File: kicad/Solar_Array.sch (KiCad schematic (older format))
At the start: 26 parts, among them IC1 SPV1040, P1 PV_CELL, P2 CONN_01X07, Q1 Q_NPN_BCE, U1 LTC2990

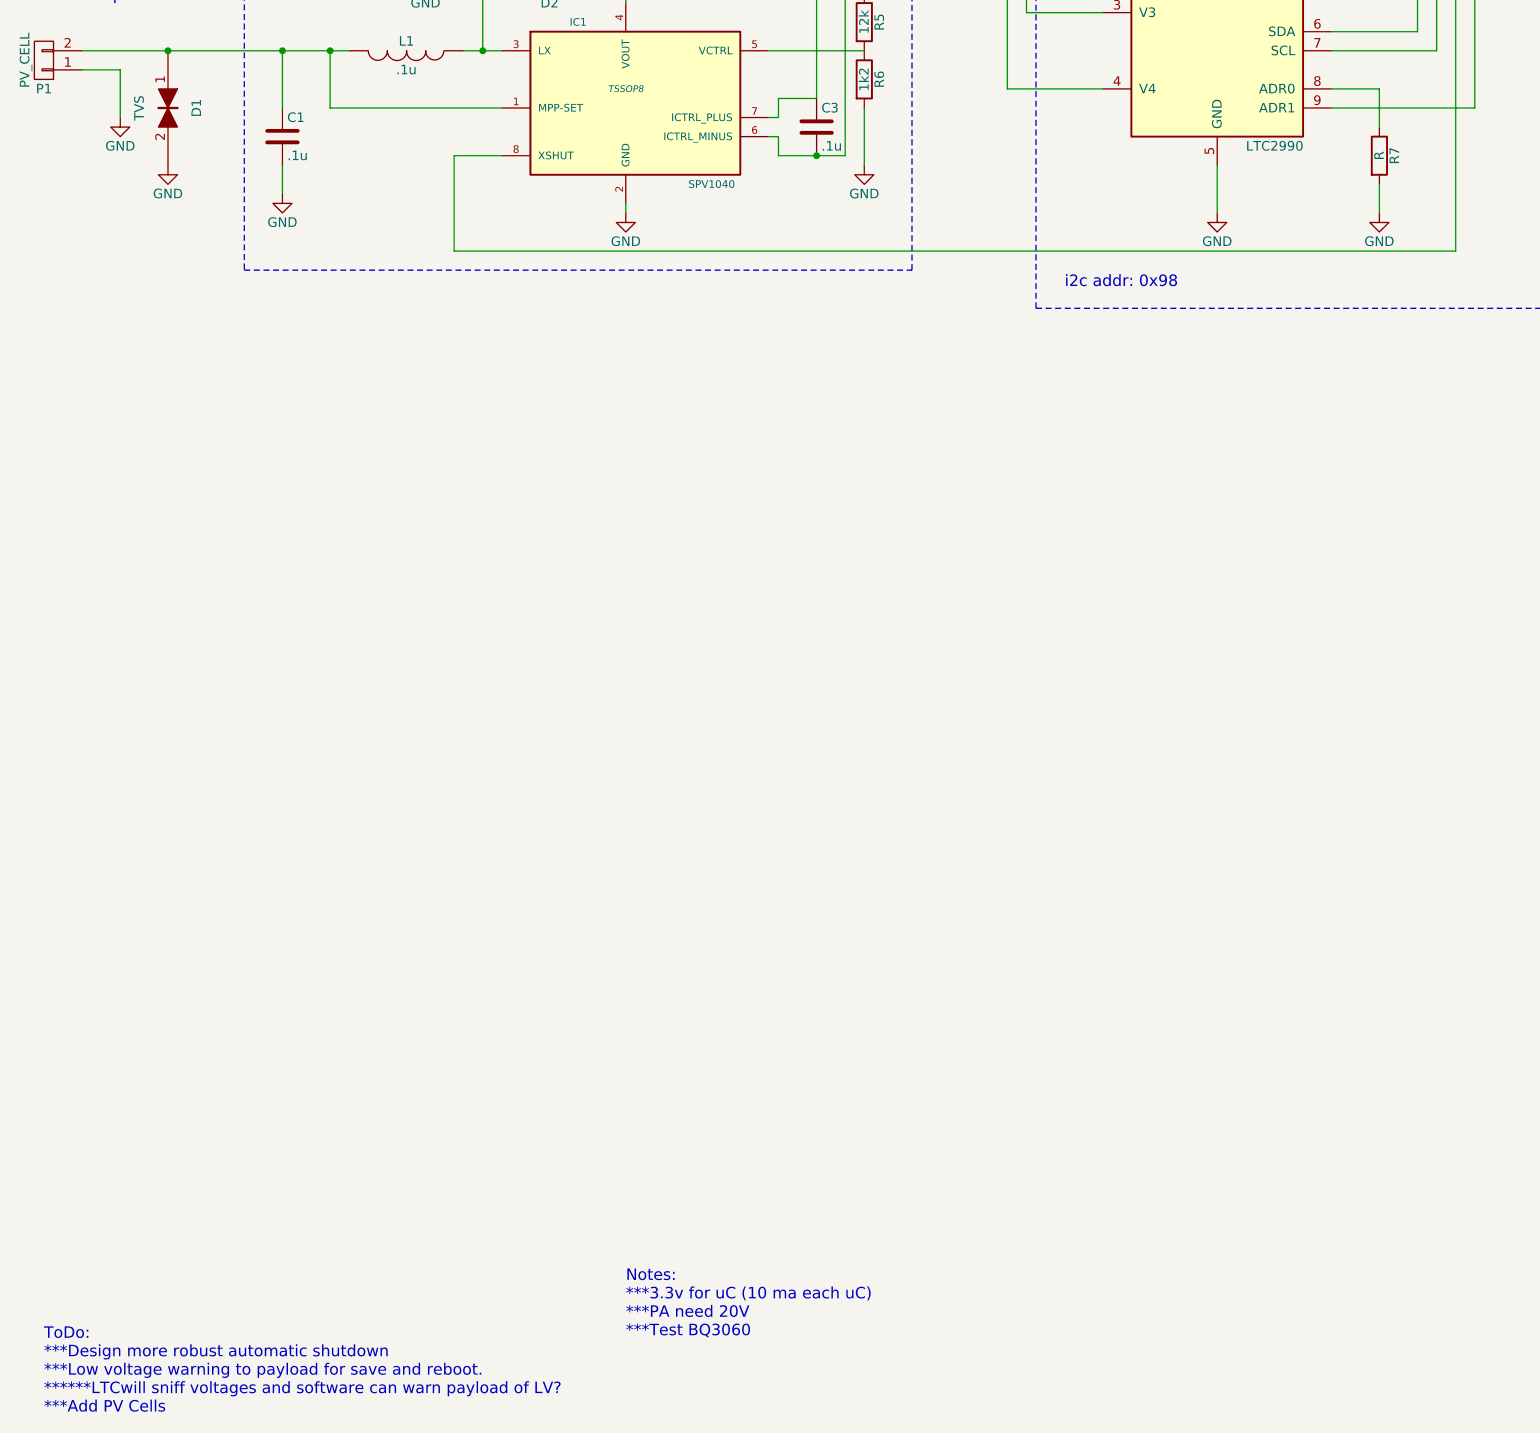
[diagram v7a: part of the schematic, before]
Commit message: Update component values, generated netlist, changed notes.
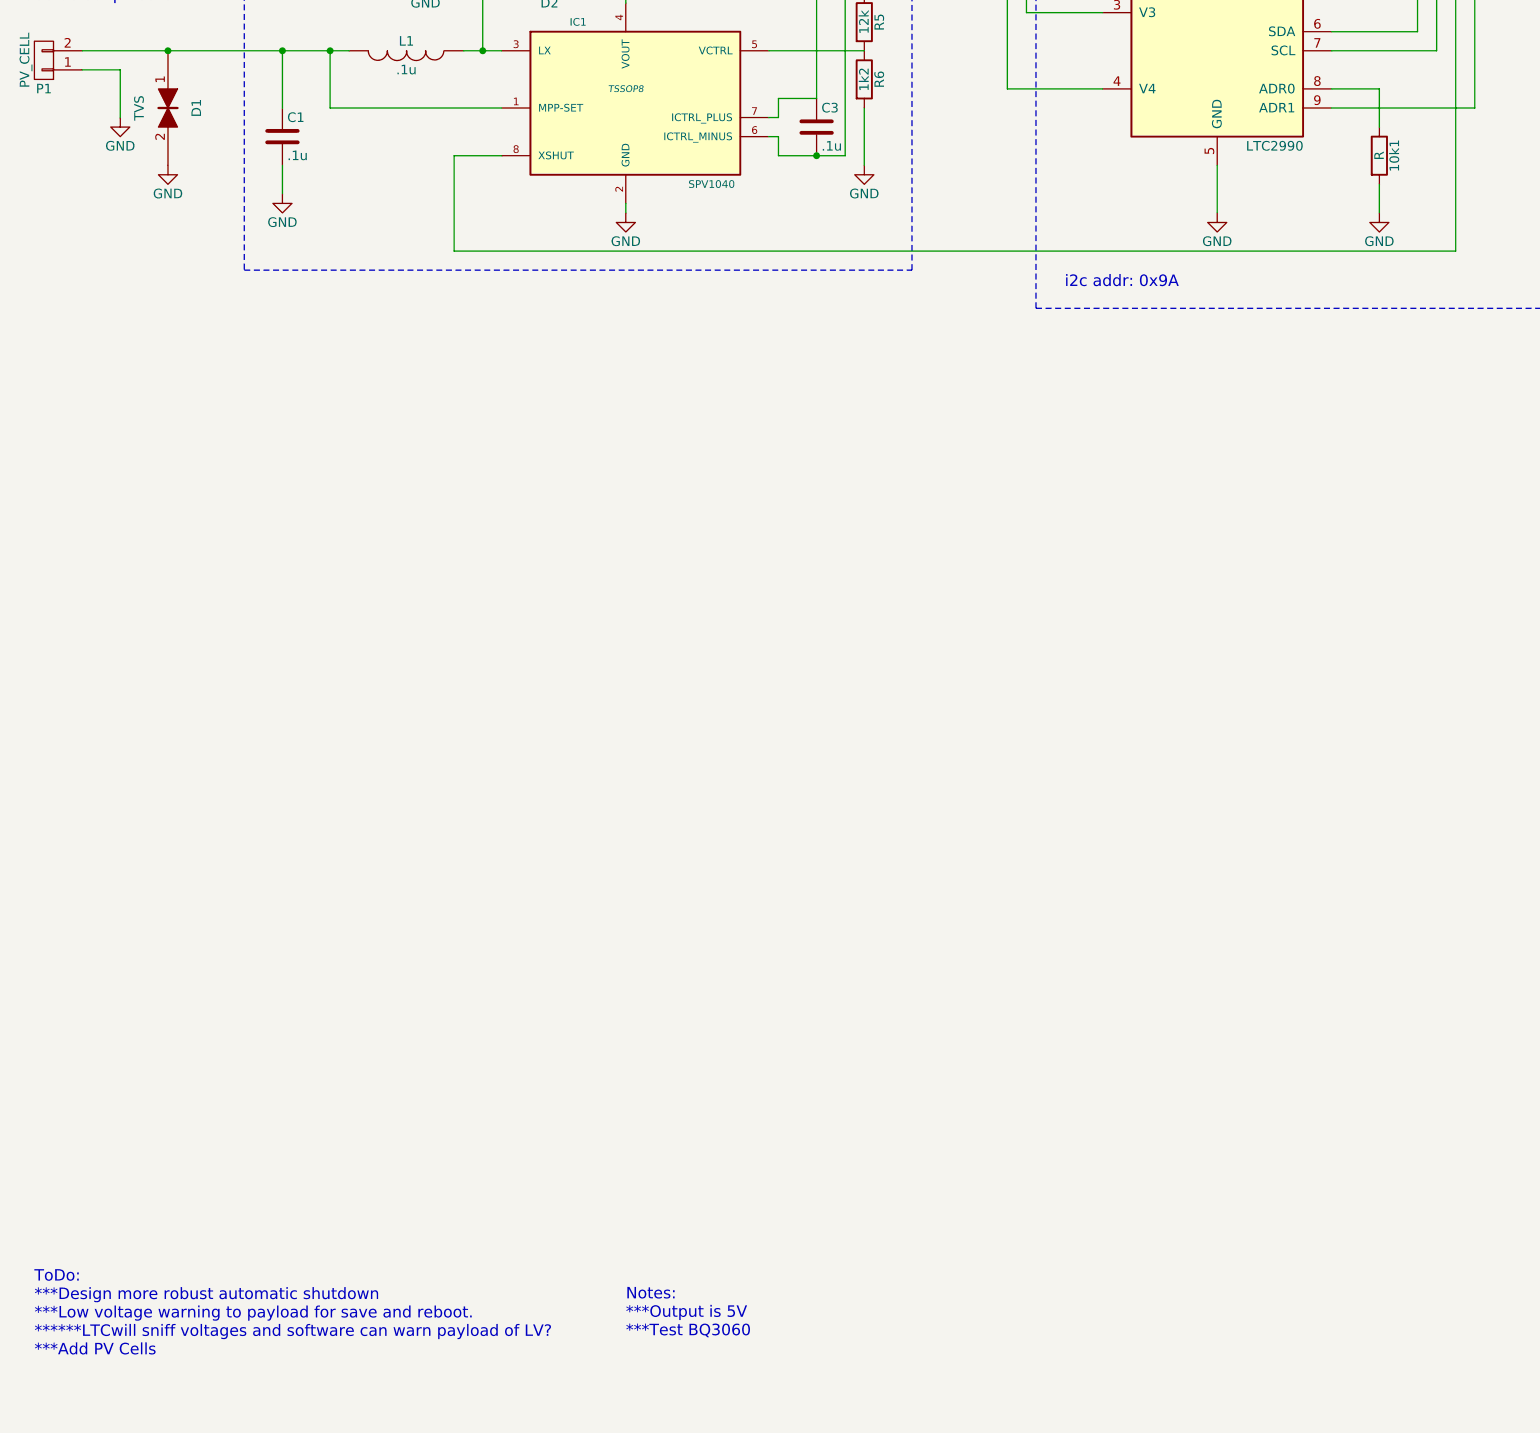
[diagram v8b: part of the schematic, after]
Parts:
- renumbered R7 to 10k1
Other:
- note added: "Notes:\n***Output is 5V\n***Test BQ3060"
- note added: "i2c addr: 0x9A"
- note removed: "Notes:\n***3.3v for uC (10 ma each uC)\n***PA need 20V\n***Test BQ3060"
- note removed: "i2c addr: 0x98"
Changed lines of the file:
@@
 $EndComp
 $Comp
-L GND #PWR7
+L GND #PWR01
 U 1 1 56A7969A
 P 7000 3600
-F 0 "#PWR7" H 7000 3350 50  0001 C CNN
+F 0 "#PWR01" H 7000 3350 50  0001 C CNN
 F 1 "GND" H 7000 3450 50  0000 C CNN
 F 2 "" H 7000 3600 60  0000 C CNN
@@
 $EndComp
 Text Notes 6200 4000 0    60   ~ 0
-i2c addr: 0x98
+i2c addr: 0x9A
 $Comp
 L R4T R1
@@
 	0    1    1    0
 $EndComp
-Text Notes 850  9900 0    60   ~ 0
+Text Notes 800  9600 0    60   ~ 0
 ToDo:\n***Design more robust automatic shutdown\n***Low voltage warning to payload for save and reboot.\n******LTCwill sniff voltages and software can warn payload of LV?\n***Add PV Cells
 Text Notes 3750 1250 1    60   ~ 0
 1%
 $Comp
-L GND #PWR1
+L GND #PWR02
 U 1 1 56A96BD7
 P 1250 3100
-F 0 "#PWR1" H 1250 2850 50  0001 C CNN
+F 0 "#PWR02" H 1250 2850 50  0001 C CNN
 F 1 "GND" H 1250 2950 50  0000 C CNN
 F 2 "" H 1250 3100 60  0000 C CNN
@@
 $EndComp
 $Comp
-L GND #PWR3
+L GND #PWR03
 U 1 1 56A97606
 P 2100 3500
-F 0 "#PWR3" H 2100 3250 50  0001 C CNN
+F 0 "#PWR03" H 2100 3250 50  0001 C CNN
 F 1 "GND" H 2100 3350 50  0000 C CNN
 F 2 "" H 2100 3500 60  0000 C CNN
@@
 $EndComp
 $Comp
-L GND #PWR6
+L GND #PWR04
 U 1 1 56A97B91
 P 5150 3350
-F 0 "#PWR6" H 5150 3100 50  0001 C CNN
+F 0 "#PWR04" H 5150 3100 50  0001 C CNN
 F 1 "GND" H 5150 3200 50  0000 C CNN
 F 2 "" H 5150 3350 60  0000 C CNN
@@
 $EndComp
 $Comp
-L GND #PWR5
+L GND #PWR05
 U 1 1 56A99359
 P 3900 3600
-F 0 "#PWR5" H 3900 3350 50  0001 C CNN
+F 0 "#PWR05" H 3900 3350 50  0001 C CNN
 F 1 "GND" H 3900 3450 50  0000 C CNN
 F 2 "" H 3900 3600 60  0000 C CNN
@@
 $EndComp
 $Comp
-L GND #PWR9
+L GND #PWR06
 U 1 1 56A9DF6A
 P 9150 1750
-F 0 "#PWR9" H 9150 1500 50  0001 C CNN
+F 0 "#PWR06" H 9150 1500 50  0001 C CNN
 F 1 "GND" H 9150 1600 50  0000 C CNN
 F 2 "" H 9150 1750 60  0000 C CNN
@@
 VCC_IN
 Text Notes 3900 9500 0    60   ~ 0
-Notes:\n***3.3v for uC (10 ma each uC)\n***PA need 20V\n***Test BQ3060
+Notes:\n***Output is 5V\n***Test BQ3060
 Text Notes 11200 950  0    50   ~ 0
 V_OUT
@@
 $EndComp
 $Comp
-L GND #PWR8
+L GND #PWR07
 U 1 1 56BAE8DD
 P 7850 3600
-F 0 "#PWR8" H 7850 3350 50  0001 C CNN
+F 0 "#PWR07" H 7850 3350 50  0001 C CNN
 F 1 "GND" H 7850 3450 50  0000 C CNN
 F 2 "" H 7850 3600 50  0000 C CNN
@@
 $EndComp
 $Comp
-L GND #PWR2
+L GND #PWR08
 U 1 1 56BB9B10
 P 1500 3350
-F 0 "#PWR2" H 1500 3100 50  0001 C CNN
+F 0 "#PWR08" H 1500 3100 50  0001 C CNN
 F 1 "GND" H 1500 3200 50  0000 C CNN
 F 2 "" H 1500 3350 50  0000 C CNN
@@
 Connection ~ 10500 2350
 $Comp
-L GND #PWR10
+L GND #PWR09
 U 1 1 56BBC663
 P 10000 2350
-F 0 "#PWR10" H 10000 2100 50  0001 C CNN
+F 0 "#PWR09" H 10000 2100 50  0001 C CNN
 F 1 "GND" H 10000 2200 50  0000 C CNN
 F 2 "" H 10000 2350 50  0000 C CNN
@@
 shunt
 $Comp
-L GND #PWR4
+L GND #PWR010
 U 1 1 56BBD7C0
 P 2850 2350
-F 0 "#PWR4" H 2850 2100 50  0001 C CNN
+F 0 "#PWR010" H 2850 2100 50  0001 C CNN
 F 1 "GND" H 2850 2200 50  0000 C CNN
 F 2 "" H 2850 2350 50  0000 C CNN
@@
 	2850 1950 2850 2050
 $Comp
-L R R7
+L R 10k1
 U 1 1 56BCEAEC
 P 7850 3300
-F 0 "R7" V 7930 3300 50  0000 C CNN
+F 0 "10k1" V 7930 3300 50  0000 C CNN
 F 1 "R" V 7850 3300 50  0000 C CNN
 F 2 "" V 7780 3300 50  0000 C CNN
